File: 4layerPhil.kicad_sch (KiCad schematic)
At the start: 59 parts, among them J1 USB_C_Receptacle_USB2.0_16P, J2 Conn_01x05_Pin, J3 Conn_01x04_Pin, J4 MEM2061-01-188-00-A_REVA, J6 1140084168, SW1 SW_SPDT, SW2 BTN1, SW3 BTN2, SW4 BTN3, U2 USBLC6-2SC6, U3 STM32F103RCTx, U4 SPX3819M5-L-3-3, Y1 16MHz

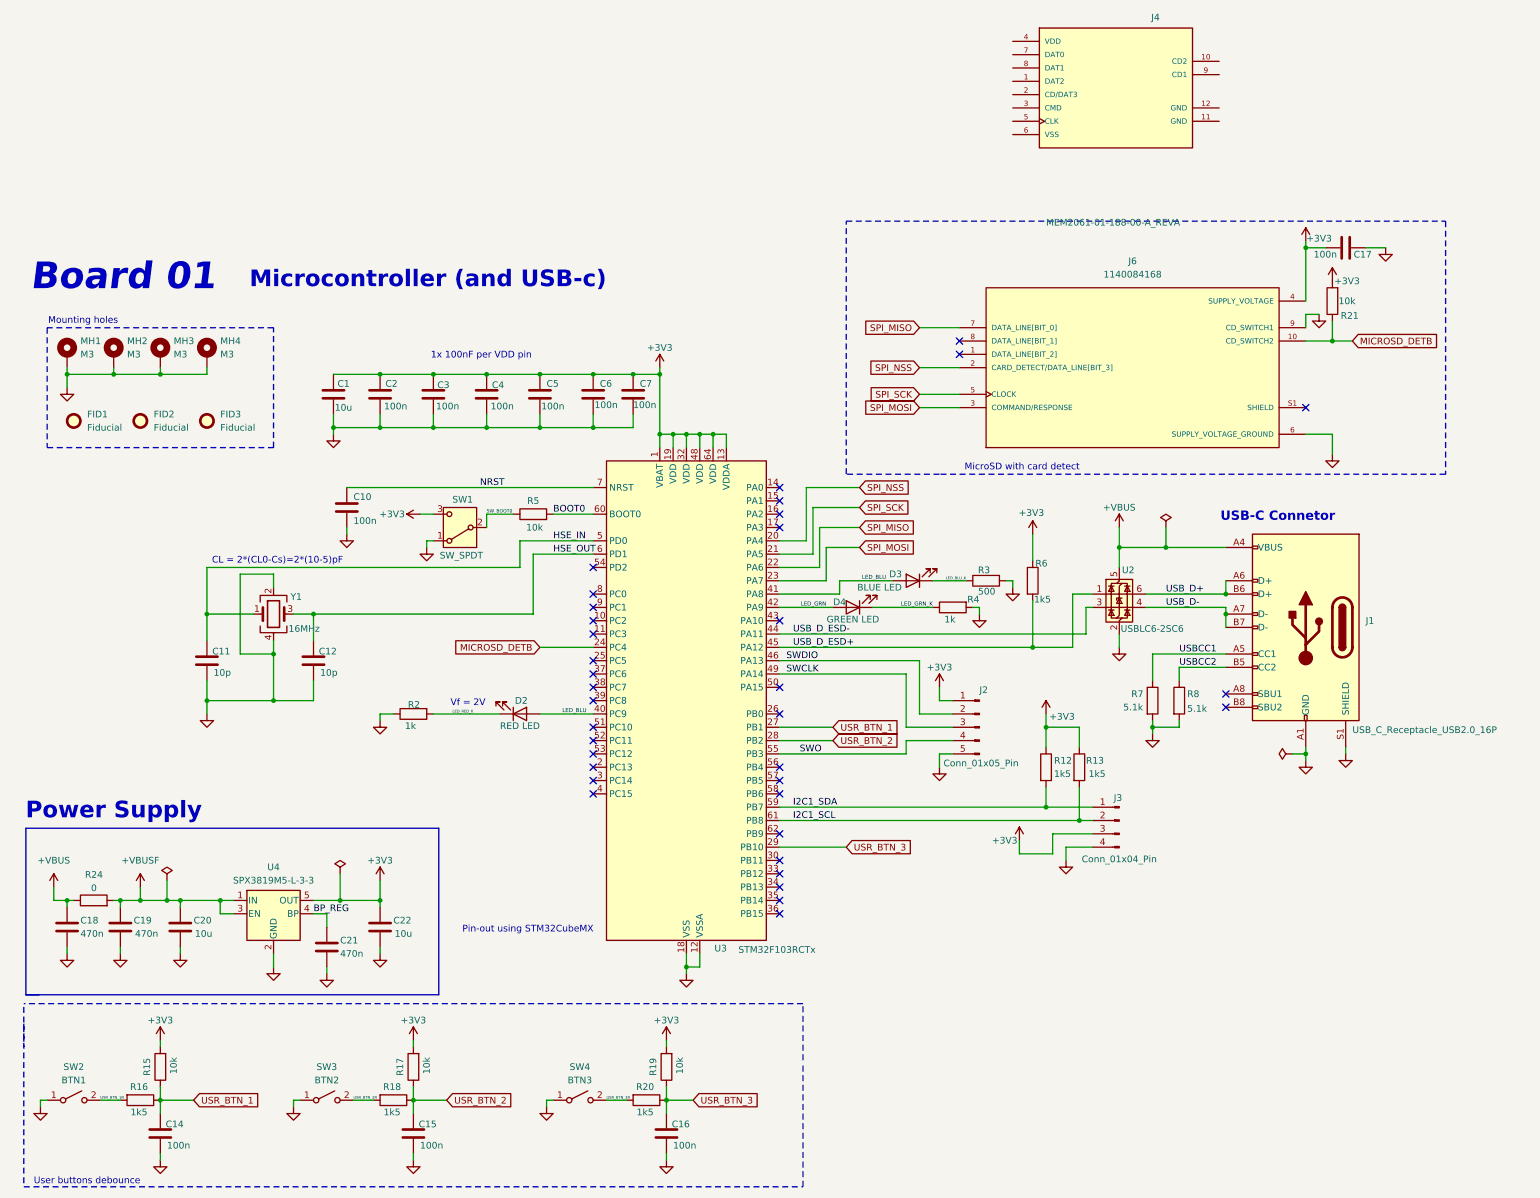
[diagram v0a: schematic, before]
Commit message: Managed to make the PCB ~5 mm smaller in both directions
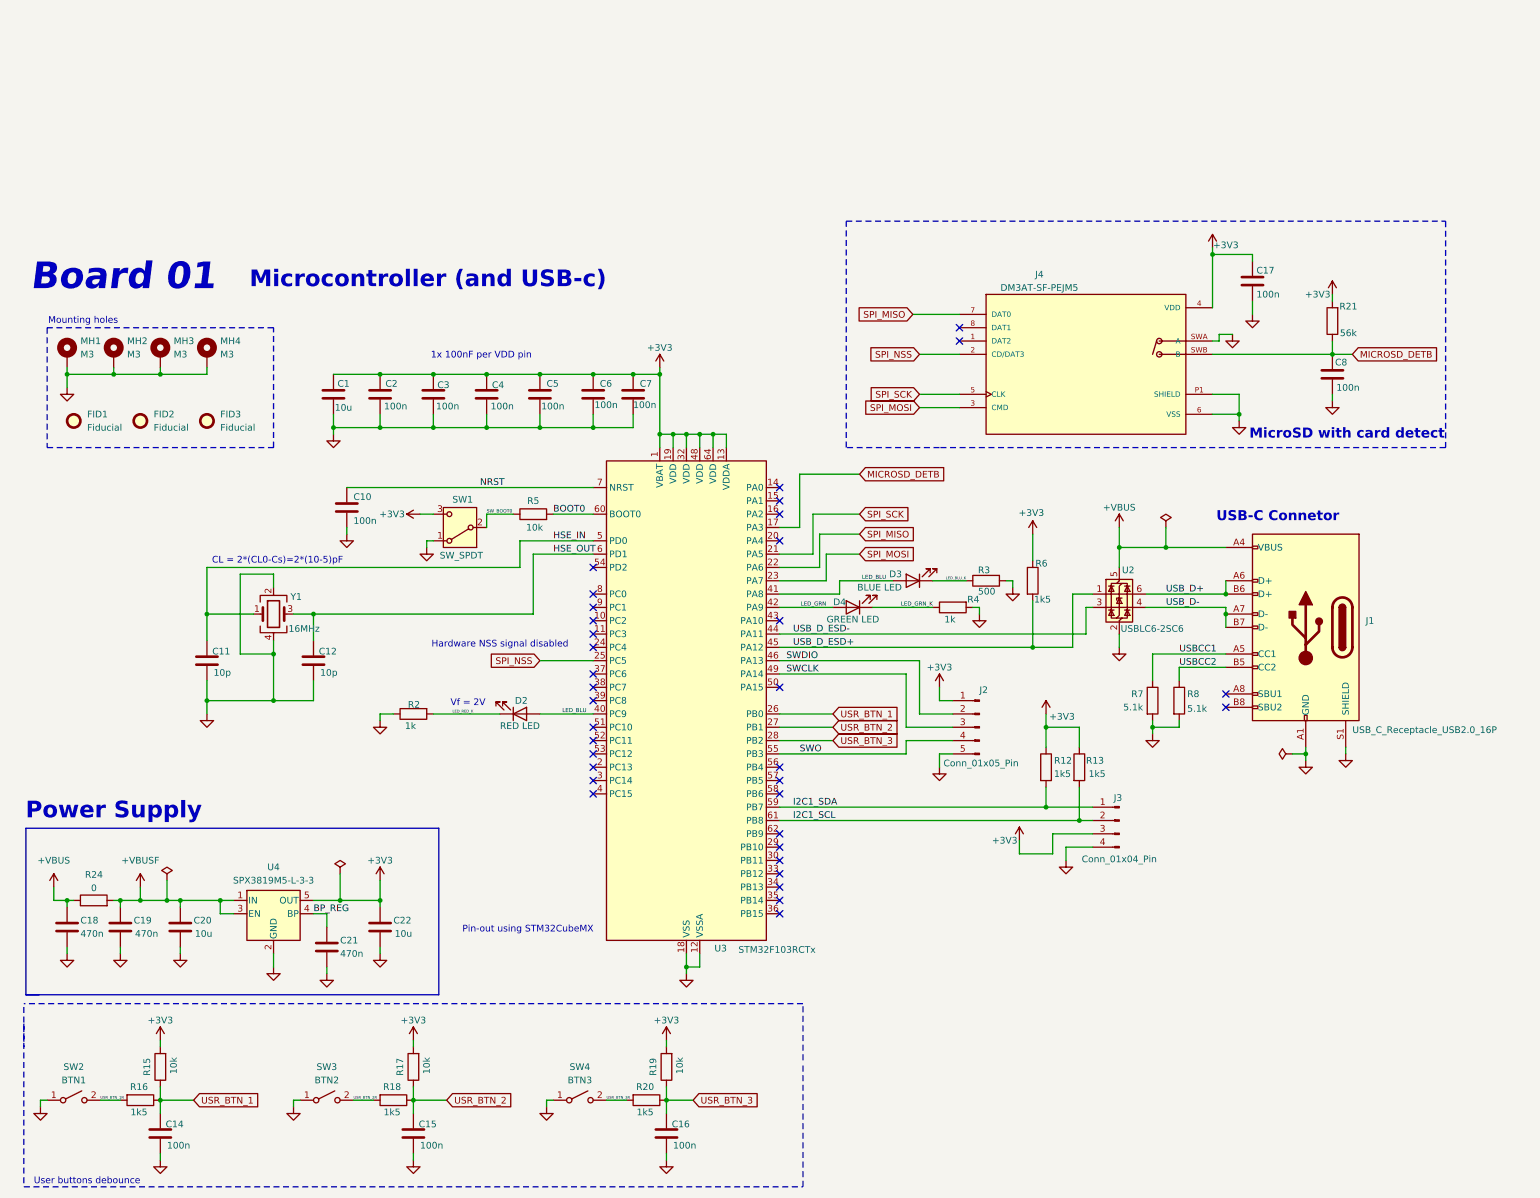
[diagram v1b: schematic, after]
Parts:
- removed J4: MEM2061-01-188-00-A_REVA, MEM2061-01-188-00-A_REVA:GCT_MEM2061-01-188-00-A_REVA, symbol MicroSD_Socket:MEM2061-01-188-00-A_REVA
- removed J6: 1140084168, MicroSD_Socket:GCT_MEM2061-01-188-00-A_REVA, symbol MicroSD_Socket:1140084168
- added C8: 100n, Capacitor_SMD:C_0603_1608Metric, symbol Device:C
- added J4: DM3AT-SF-PEJM5, microSD_DM3AT:HRS_DM3AT-SF-PEJM5, symbol microSD_DM3AT:DM3AT-SF-PEJM5
- R21: value 10k -> 56k
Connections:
- net +3V3: now also C17.1, J4.4 (VDD); no longer C17.2
- net GND: now also C17.2, C8.2, J4.6 (VSS), J4.P1 (SHIELD), J4.P2 (SHIELD), J4.P3 (SHIELD), J4.P4 (SHIELD), J4.SWA (A); no longer C17.1
- net MICROSD_DETB: now also U3.17 (PA3), C8.1, J4.SWB (B); no longer U3.24 (PC4)
- net SPI_MISO: now also J4.7 (DAT0)
- net SPI_MOSI: now also J4.3 (CMD)
- net SPI_NSS: now also U3.25 (PC5), J4.2 (CD/DAT3); no longer U3.20 (PA4)
- net SPI_SCK: now also J4.5 (CLK)
- net USR_BTN_1: now also U3.26 (PB0); no longer U3.27 (PB1)
- net USR_BTN_2: now also U3.27 (PB1); no longer U3.28 (PB2)
- net USR_BTN_3: now also U3.28 (PB2); no longer U3.29 (PB10)
- no-connect marks 36 -> 35
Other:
- note added: "Hardware NSS signal disabled"
- moved on the sheet: C17, R21

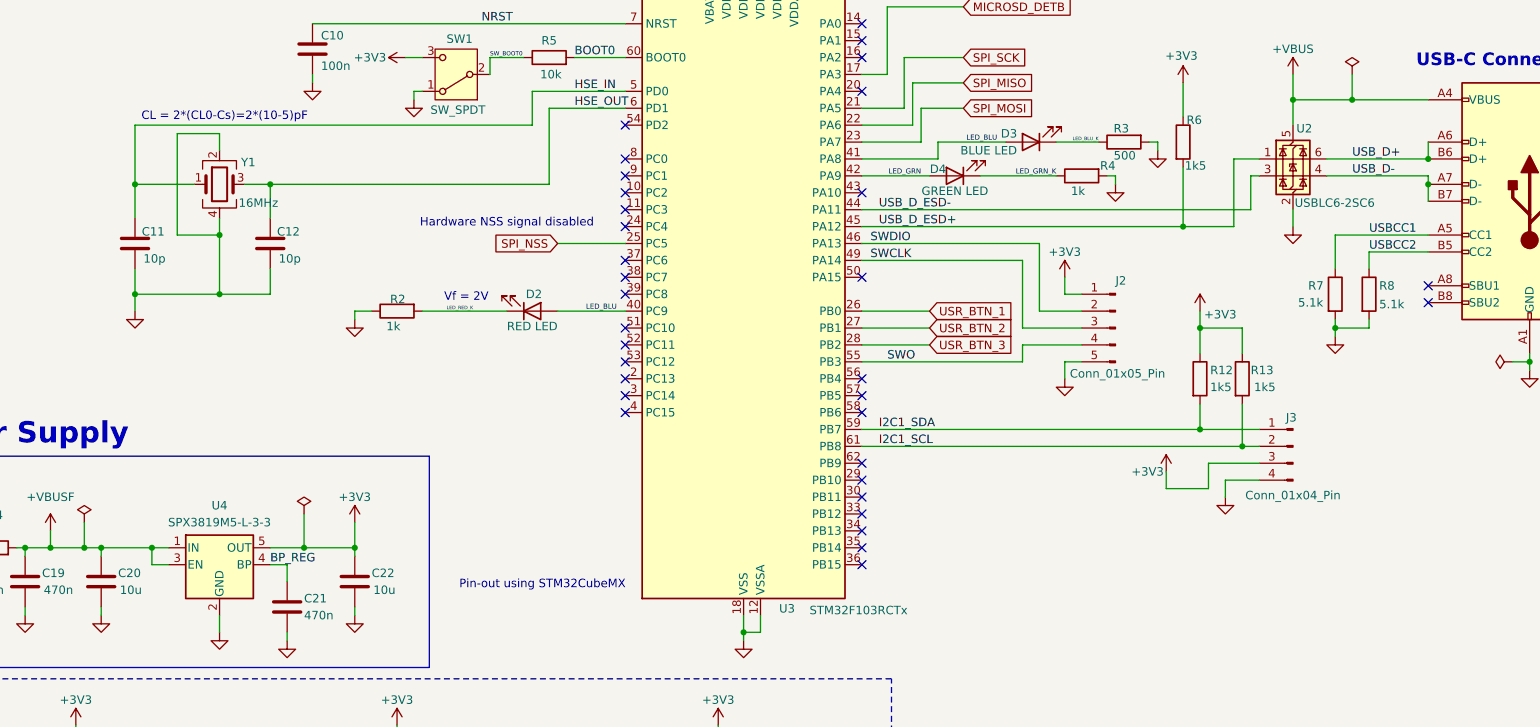
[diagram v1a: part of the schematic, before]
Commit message: Finished signal routing and layout, started power routing
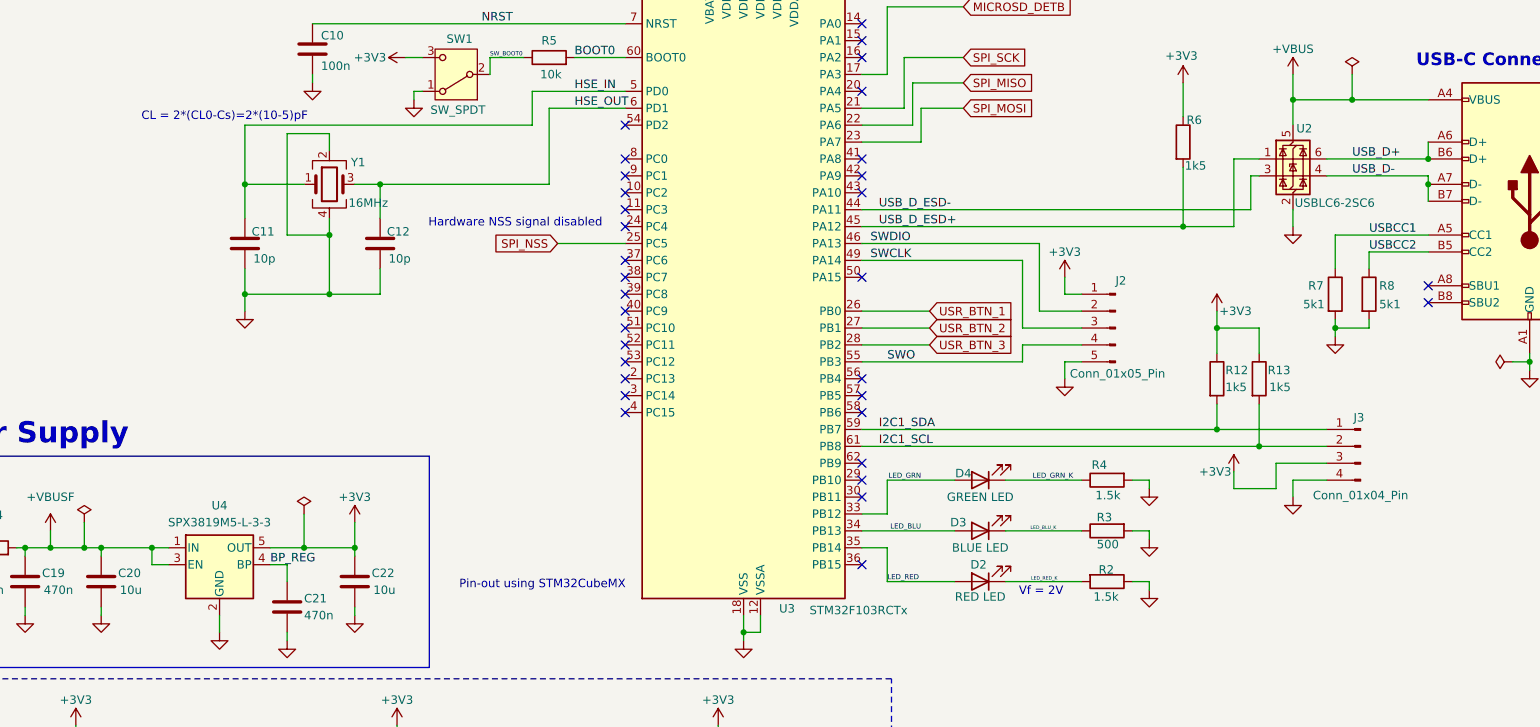
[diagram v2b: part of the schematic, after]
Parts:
- R2, R4: value 1k -> 1.5k
- R7, R8: value 5.1k -> 5k1
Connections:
- net LED_BLU: now also U3.34 (PB13); no longer D2.2 (A), U3.40 (PC9), U3.41 (PA8)
- net LED_GRN: now also U3.33 (PB12); no longer U3.42 (PA9)
- net LED_RED: now reaches U3.35 (PB14)
- net LED_RED: now also D2.2 (A)
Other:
- moved on the sheet: C11, C12, D2, D3, D4, J3, R12, R13, R2, R3, R4, Y1

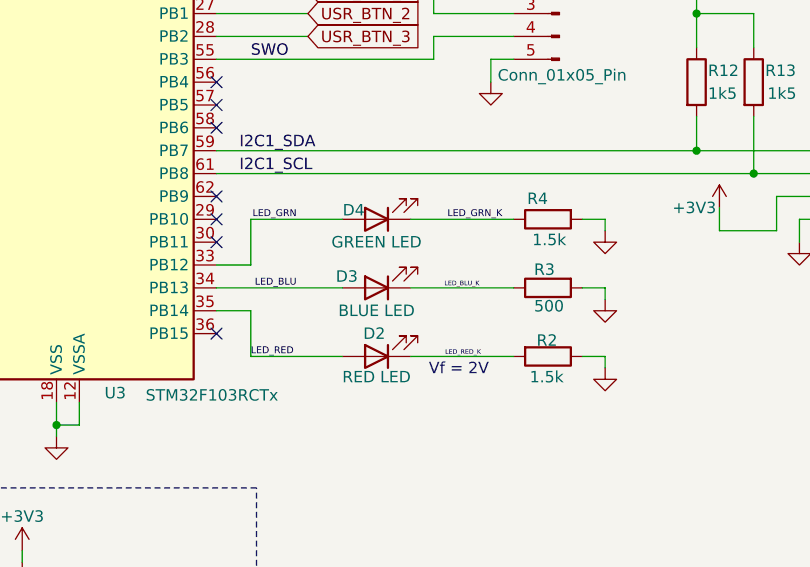
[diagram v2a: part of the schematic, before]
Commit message: Finished pcb routing and layout but preparing to change the regulator to a buck converter for better thermals
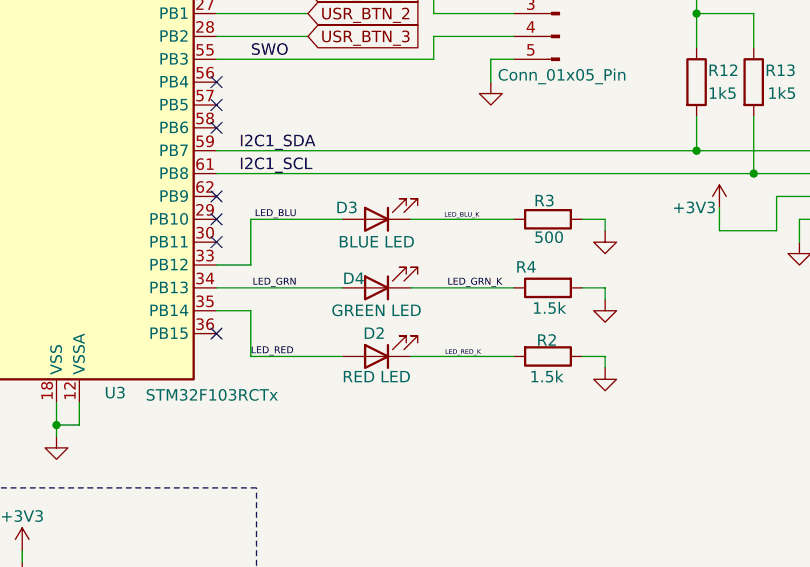
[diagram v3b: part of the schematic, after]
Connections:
- net LED_BLU: now also U3.33 (PB12); no longer U3.34 (PB13)
- net LED_GRN: now also U3.34 (PB13); no longer U3.33 (PB12)
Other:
- note removed: "Vf = 2V"
- moved on the sheet: D3, D4, R3, R4

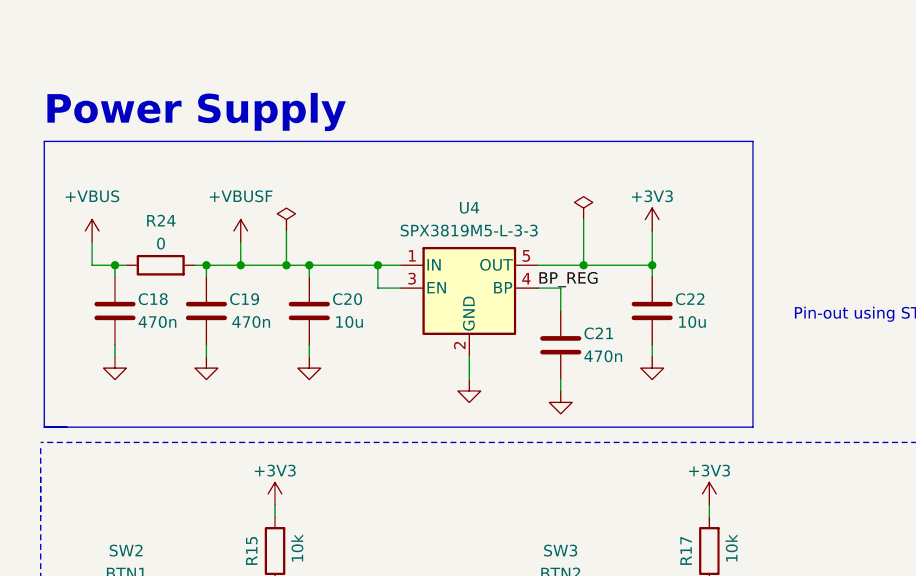
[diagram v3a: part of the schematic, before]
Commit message: Removed LDO in favour of Buck converter, assigned footprints, ready to layout on the PCB
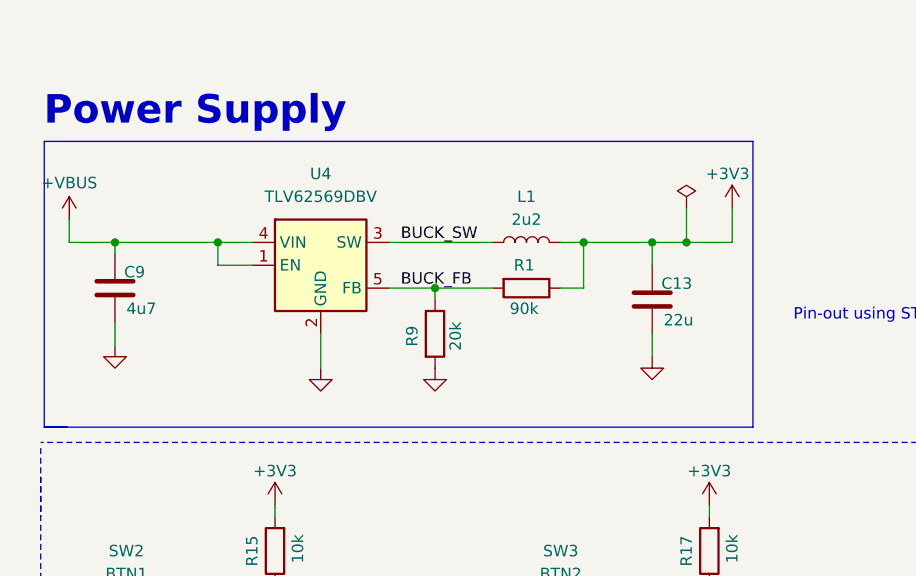
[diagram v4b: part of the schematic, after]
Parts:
- removed C18, C19, C21: 470n, Capacitor_SMD:C_0603_1608Metric, symbol Device:C
- removed C20, C22: 10u, Capacitor_SMD:C_0805_2012Metric, symbol Device:C
- removed R24: 0, Resistor_SMD:R_0603_1608Metric, symbol Device:R
- removed U4: SPX3819M5-L-3-3, Package_TO_SOT_SMD:SOT-23-5, symbol Regulator_Linear:SPX3819M5-L-3-3
- added C13: 22u, Capacitor_SMD:C_0805_2012Metric, symbol Device:C
- added C9: 4u7, Capacitor_SMD:C_0805_2012Metric, symbol Device:C
- added L1: 2u2, Inductor_SMD:L_0805_2012Metric, symbol Device:L
- added R1: 90k, Resistor_SMD:R_0603_1608Metric, symbol Device:R
- added R9: 20k, Resistor_SMD:R_0603_1608Metric, symbol Device:R
- added U4: TLV62569DBV, Package_TO_SOT_SMD:SOT-23-5, symbol Regulator_Switching:TLV62569DBV
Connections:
- net +3V3: now also C13.1, L1.2, R1.1
- net +VBUS: now also C9.1, U4.1 (EN), U4.4 (VIN)
- net GND: now also C13.2, C9.2, R9.2, U4.2 (GND)
- new net BUCK_FB: R1.2, R9.1, U4.5 (FB)
- new net BUCK_SW: L1.1, U4.3 (SW)

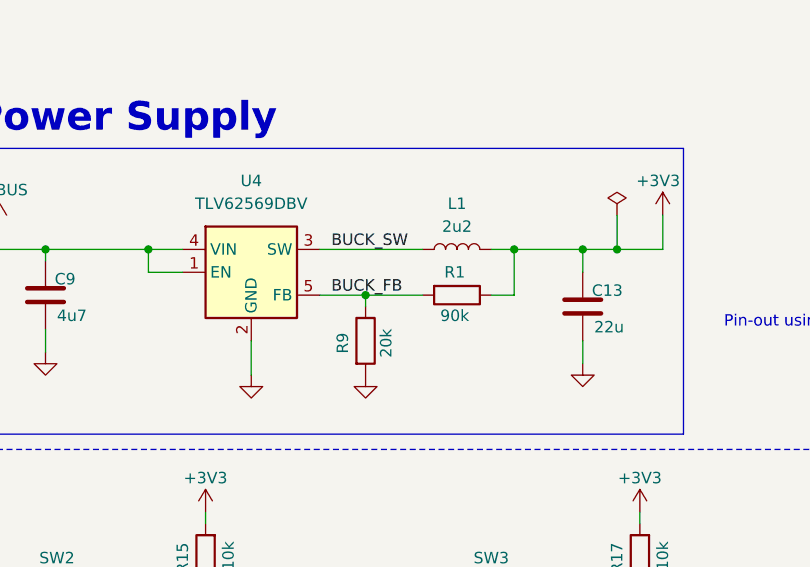
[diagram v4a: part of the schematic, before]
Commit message: Added LM3671MF buck converter
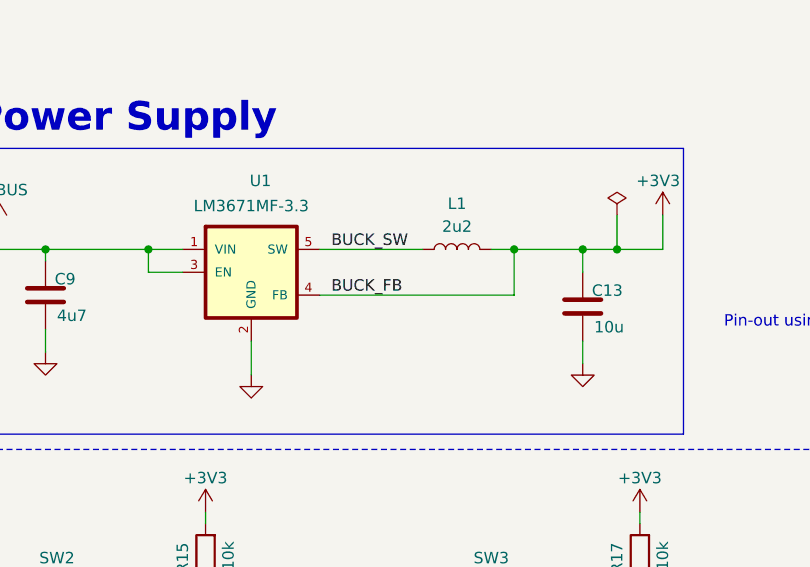
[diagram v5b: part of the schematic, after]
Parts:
- removed R1: 90k, Resistor_SMD:R_0603_1608Metric, symbol Device:R
- removed R9: 20k, Resistor_SMD:R_0603_1608Metric, symbol Device:R
- removed U4: TLV62569DBV, Package_TO_SOT_SMD:SOT-23-5, symbol Regulator_Switching:TLV62569DBV
- added U1: LM3671MF-3.3, Buck_LM3671:SOT95P280X145-5N, symbol Buck_LM3671:LM3671MF-3.3
- C13: value 22u -> 10u
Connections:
- net +3V3: now also U1.4 (FB)
- net +VBUS: now also U1.1 (VIN), U1.3 (EN)
- net BUCK_SW: now also U1.5 (SW)
- net GND: now also U1.2 (GND)
